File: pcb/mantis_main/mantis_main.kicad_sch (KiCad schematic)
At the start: 97 parts, among them J1 Conn_01x02_Socket, M1 SW_Mouse, M2 SW_Mouse, SW1 SW_SPDT, U1 74LVC1G17

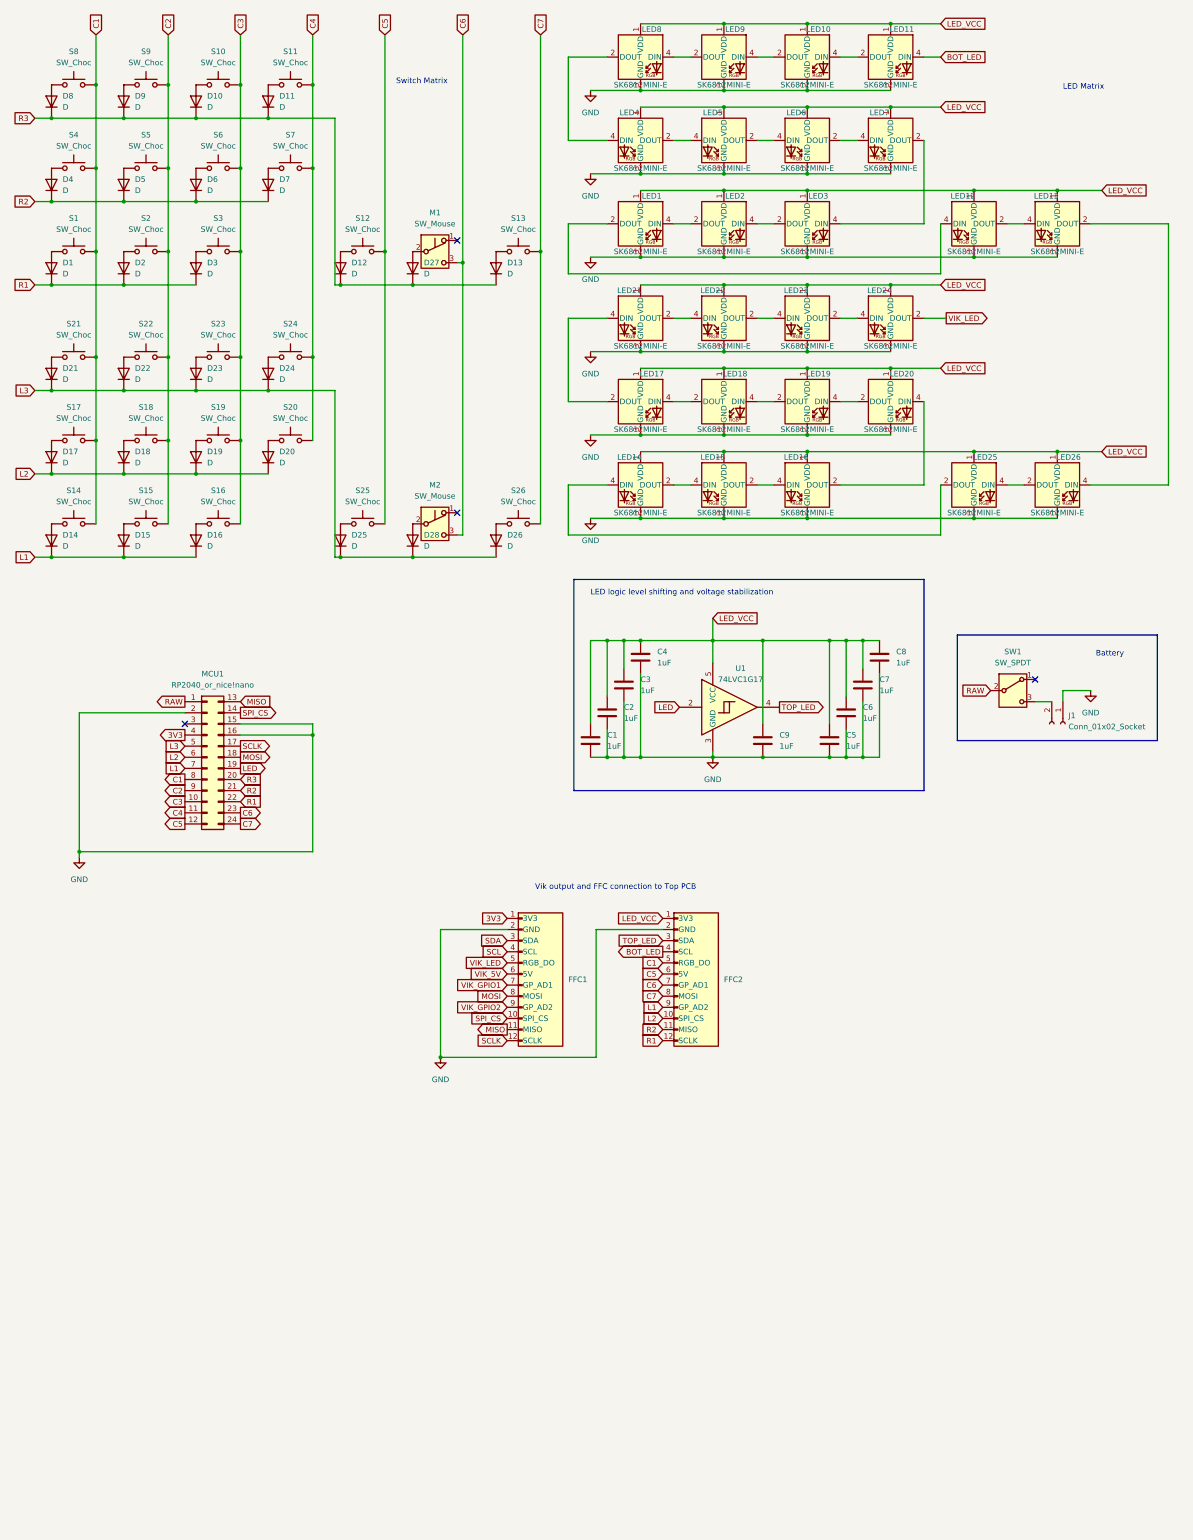
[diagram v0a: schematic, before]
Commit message: Added jumpers and screen connectors to schematic
For configuring the PCB for different controllers, display/LED setups and
protocols for connecting sensors.

Signed-off-by: Felix Kuehling <felix.kuehling@gmail.com>
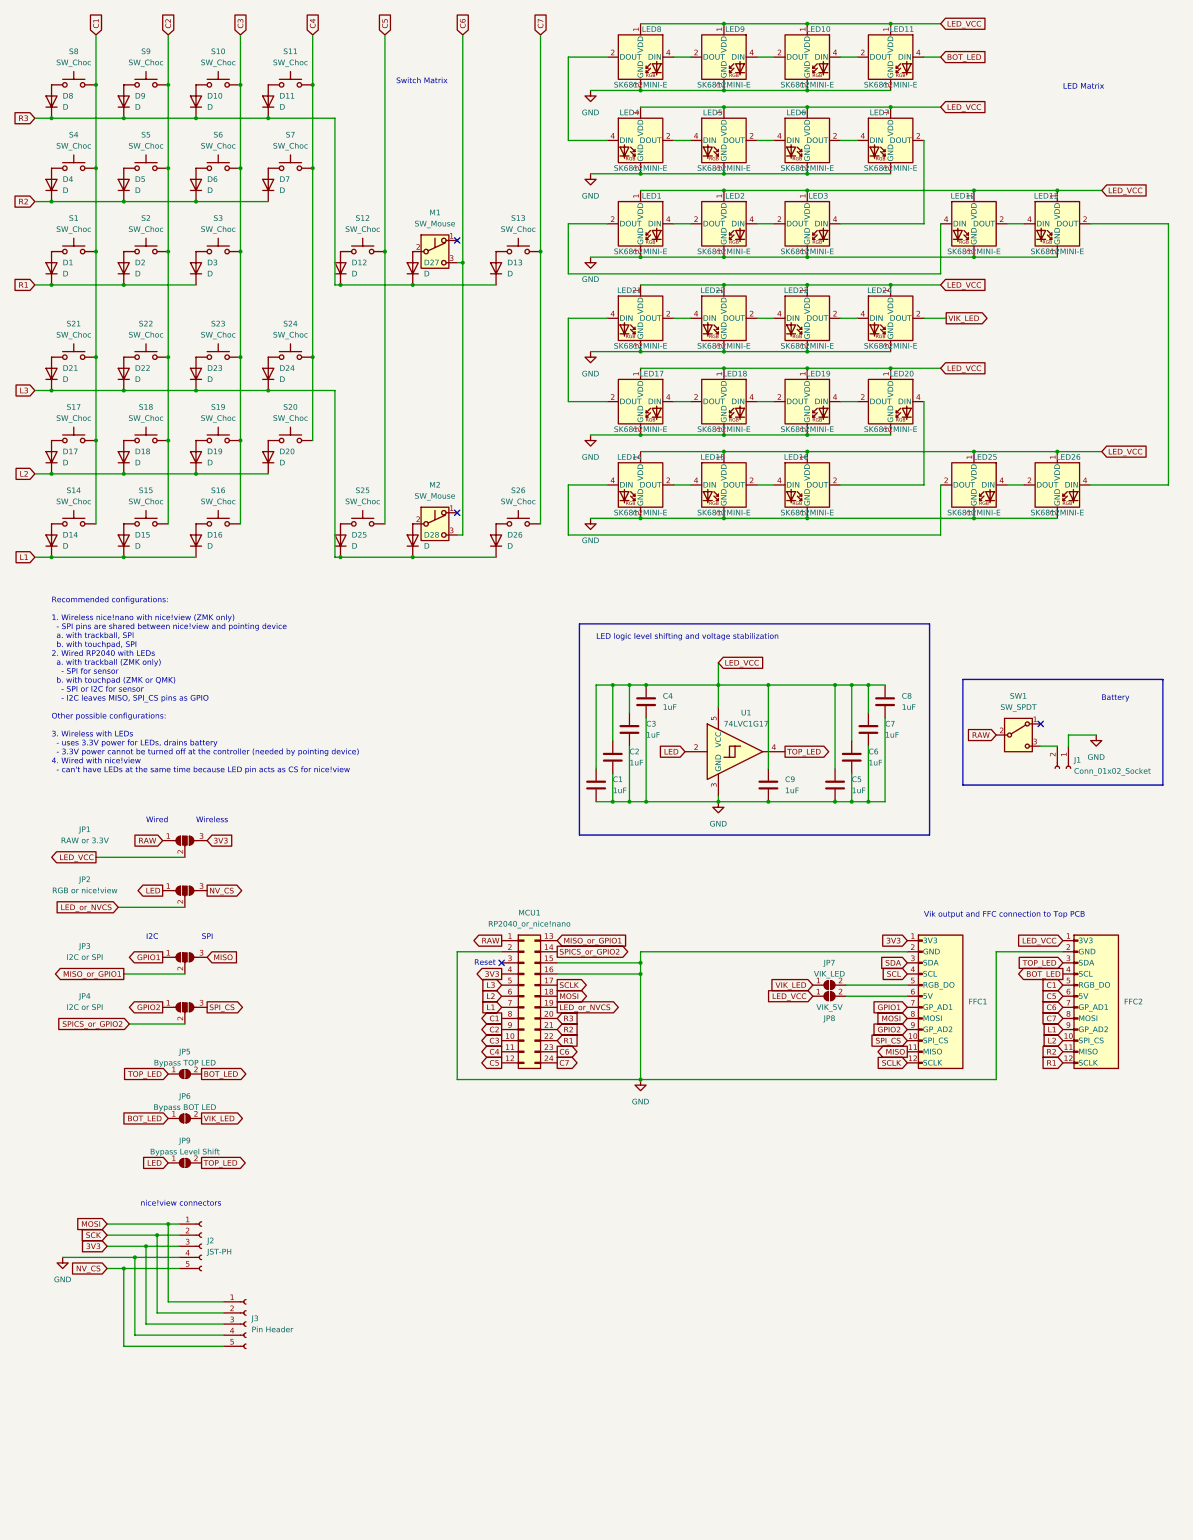
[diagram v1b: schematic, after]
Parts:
- added J2: JST-PH, Connector_JST:JST_PH_S5B-PH-K_1x05_P2.00mm_Horizontal, symbol Connector:Conn_01x05_Socket
- added J3: Pin Header, Connector_PinSocket_2.54mm:PinSocket_1x05_P2.54mm_Vertical, symbol Connector:Conn_01x05_Socket
- added JP1: RAW or 3.3V, Jumper:SolderJumper-3_P2.0mm_Open_TrianglePad1.0x1.5mm, symbol Jumper:SolderJumper_3_Open
- added JP2: RGB or nice!view, Jumper:SolderJumper-3_P2.0mm_Open_TrianglePad1.0x1.5mm, symbol Jumper:SolderJumper_3_Open
- added JP3, JP4: I2C or SPI, Jumper:SolderJumper-3_P2.0mm_Open_TrianglePad1.0x1.5mm, symbol Jumper:SolderJumper_3_Open
- added JP5: Bypass TOP LED, Jumper:SolderJumper-2_P1.3mm_Open_TrianglePad1.0x1.5mm, symbol Jumper:SolderJumper_2_Open
- added JP6: Bypass BOT LED, Jumper:SolderJumper-2_P1.3mm_Open_TrianglePad1.0x1.5mm, symbol Jumper:SolderJumper_2_Open
- added JP7: VIK_LED, Jumper:SolderJumper-2_P1.3mm_Open_TrianglePad1.0x1.5mm, symbol Jumper:SolderJumper_2_Open
- added JP8: VIK_5V, Jumper:SolderJumper-2_P1.3mm_Open_TrianglePad1.0x1.5mm, symbol Jumper:SolderJumper_2_Open
- added JP9: Bypass Level Shift, Jumper:SolderJumper-2_P1.3mm_Open_TrianglePad1.0x1.5mm, symbol Jumper:SolderJumper_2_Open
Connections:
- net 3V3: now also J2.3 (Pin_3), J3.3 (Pin_3), JP1.3 (B)
- net BOT_LED: now also JP5.2 (B), JP6.1 (A)
- net GND: now also J2.4 (Pin_4), J3.4 (Pin_4)
- net LED: now also JP2.1 (A), JP9.1 (A); no longer MCU1.19 (Pin_19)
- net LED_VCC: now also JP1.2 (C), JP8.1 (A)
- net MISO: now also JP3.3 (B); no longer MCU1.13 (Pin_13)
- net MOSI: now also J2.1 (Pin_1), J3.1 (Pin_1)
- net RAW: now also JP1.1 (A)
- net SPI_CS: now also JP4.3 (B); no longer MCU1.14 (Pin_14)
- net TOP_LED: now also JP5.1 (A), JP9.2 (B)
- net VIK_LED: now also JP6.2 (B), JP7.1 (A); no longer FFC1.5 (RGB_DO)
- net VIK_5V: no longer names the net of FFC1.6 (5V)
- net VIK_5V: now also JP8.2 (B)
- net VIK_GPIO1 renamed GPIO1
- net GPIO1: now also JP3.1 (A)
- net VIK_GPIO2 renamed GPIO2
- net GPIO2: now also JP4.1 (A)
- new net: FFC1.5 (RGB_DO), JP7.2 (B)
- new net LED_or_NVCS: JP2.2 (C), MCU1.19 (Pin_19)
- new net MISO_or_GPIO1: JP3.2 (C), MCU1.13 (Pin_13)
- new net NV_CS: J2.5 (Pin_5), J3.5 (Pin_5), JP2.3 (B)
- new net SCK: J2.2 (Pin_2), J3.2 (Pin_2)
- new net SPICS_or_GPIO2: JP4.2 (C), MCU1.14 (Pin_14)
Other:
- note added: "I2C"
- note added: "Recommended configurations: 1. Wireless nice!nano with nice!view (ZMK only) - SPI pins are shared between nice!view and pointing device a. with trackball, SPI b. with touchpad, SPI 2. Wired RP2040 with LEDs a. with trackball (ZMK only) - SPI for sensor b. with touchpad (ZMK or QMK) - SPI or I2C for sensor - I2C leaves MISO, SPI_CS pins as GPIO Other possible configurations: 3. Wireless with LEDs 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"
- note added: "Reset"
- note added: "SPI"
- note added: "Wired"
- note added: "Wireless"
- note added: "nice!view connectors"
- moved on the sheet: C1, C2, C3, C4, C5, C6, C7, C8, C9, FFC1, FFC2, J1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

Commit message: pcb: Update main PCB schematic
- Removed C9 capacitor that's not needed
- Added resistor in front of first LED
- Added ferrite bead to protect ground pins from ESD
- Added jumpers to optionally connect SDA and SCL pins for I2C with
  optional pull-up resistors
- Added extra 3-pin header to enable SPI+I2C on nice!nano and an extra GPIO
  pin that's needed for DR by the ZMK driver for Cirque trackpads
- Updated configuration recommendations

Signed-off-by: Felix Kuehling <felix.kuehling@gmail.com>
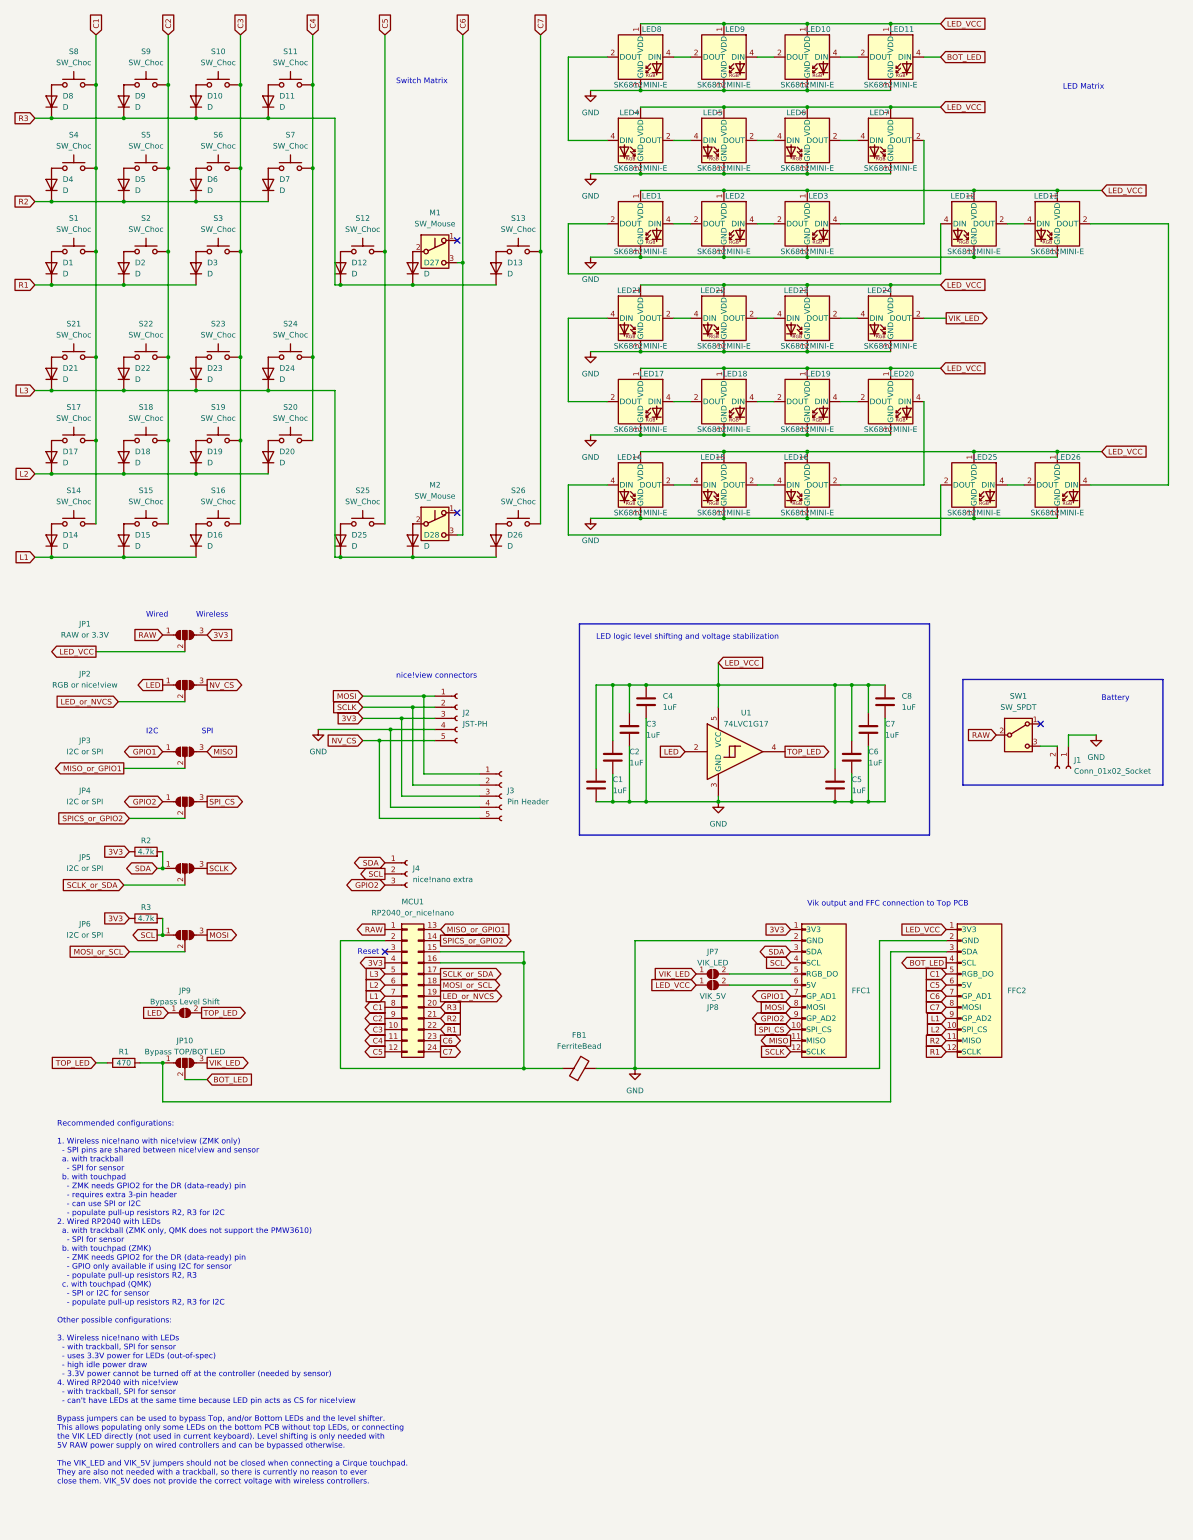
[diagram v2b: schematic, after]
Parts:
- removed C9: 1uF, Capacitor_SMD:C_0603_1608Metric, symbol Device:C
- removed JP6: Bypass BOT LED, Jumper:SolderJumper-2_P1.3mm_Open_TrianglePad1.0x1.5mm, symbol Jumper:SolderJumper_2_Open
- added FB1: FerriteBead, Capacitor_SMD:C_0805_2012Metric, symbol Device:FerriteBead
- added J4: nice!nano extra, Connector_PinSocket_2.54mm:PinSocket_1x03_P2.54mm_Vertical, symbol Connector:Conn_01x03_Socket
- added JP5, JP6: I2C or SPI, Jumper:SolderJumper-3_P2.0mm_Open_TrianglePad1.0x1.5mm, symbol Jumper:SolderJumper_3_Open
- added R1: 470, Resistor_SMD:R_0603_1608Metric, symbol Device:R
- added R2, R3: 4.7k, Resistor_SMD:R_0603_1608Metric, symbol Device:R
- JP10: renamed from JP5; value Bypass TOP LED -> Bypass TOP/BOT LED; footprint Jumper:SolderJumper-2_P1.3mm_Open_TrianglePad1.0x1.5mm -> Jumper:SolderJumper-3_P2.0mm_Open_TrianglePad1.0x1.5mm; symbol Jumper:SolderJumper_2_Open -> Jumper:SolderJumper_3_Open
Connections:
- net SCK is gone; now on net SCLK: J2.2 (Pin_2), J3.2 (Pin_2)
- net 3V3: now also R2.1, R3.1
- net GND: now also FB1.2; no longer MCU1.15 (Pin_15), MCU1.16 (Pin_16), MCU1.2 (Pin_2)
- net GPIO2: now also J4.3 (Pin_3)
- net MOSI: now also JP6.3 (B); no longer MCU1.18 (Pin_18)
- net SCL: now also J4.2 (Pin_2), JP6.1 (A), R3.2
- net SCLK: now also JP5.3 (B); no longer MCU1.17 (Pin_17)
- net SDA: now also J4.1 (Pin_1), JP5.1 (A), R2.2
- net TOP_LED: now also R1.1; no longer FFC2.3 (SDA), JP10.1 (A)
- net VIK_LED: now also JP10.3 (B)
- new net: FFC2.3 (SDA), JP10.1 (A), R1.2
- new net: FB1.1, MCU1.15 (Pin_15), MCU1.16 (Pin_16), MCU1.2 (Pin_2)
- new net MOSI_or_SCL: JP6.2 (C), MCU1.18 (Pin_18)
- new net SCLK_or_SDA: JP5.2 (C), MCU1.17 (Pin_17)
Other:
- note added: "Recommended configurations: 1. Wireless nice!nano with nice!view (ZMK only) - SPI pins are shared between nice!view and sensor a. with trackball - SPI for sensor b. with touchpad - ZMK needs GPIO2 for the DR (data-ready) pin - requires extra 3-pin header - can use SPI or I2C - populate pull-up resistors R2, R3 for I2C 2. Wired RP2040 with LEDs a. with trackball (ZMK only, QMK does not support the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"
- note removed: "Recommended configurations: 1. Wireless nice!nano with nice!view (ZMK only) - SPI pins are shared between nice!view and pointing device a. with trackball, SPI b. with touchpad, SPI 2. Wired RP2040 with LEDs a. with trackball (ZMK only) - SPI for sensor b. with touchpad (ZMK or QMK) - SPI or I2C for sensor - I2C leaves MISO, SPI_CS pins as GPIO Other possible configurations: 3. Wireless with LEDs 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"
- moved on the sheet: FFC1, FFC2, J2, J3, JP1, JP2, JP3, JP4, JP7, JP8, JP9, MCU1
